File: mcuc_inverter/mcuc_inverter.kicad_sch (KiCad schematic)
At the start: 0 parts

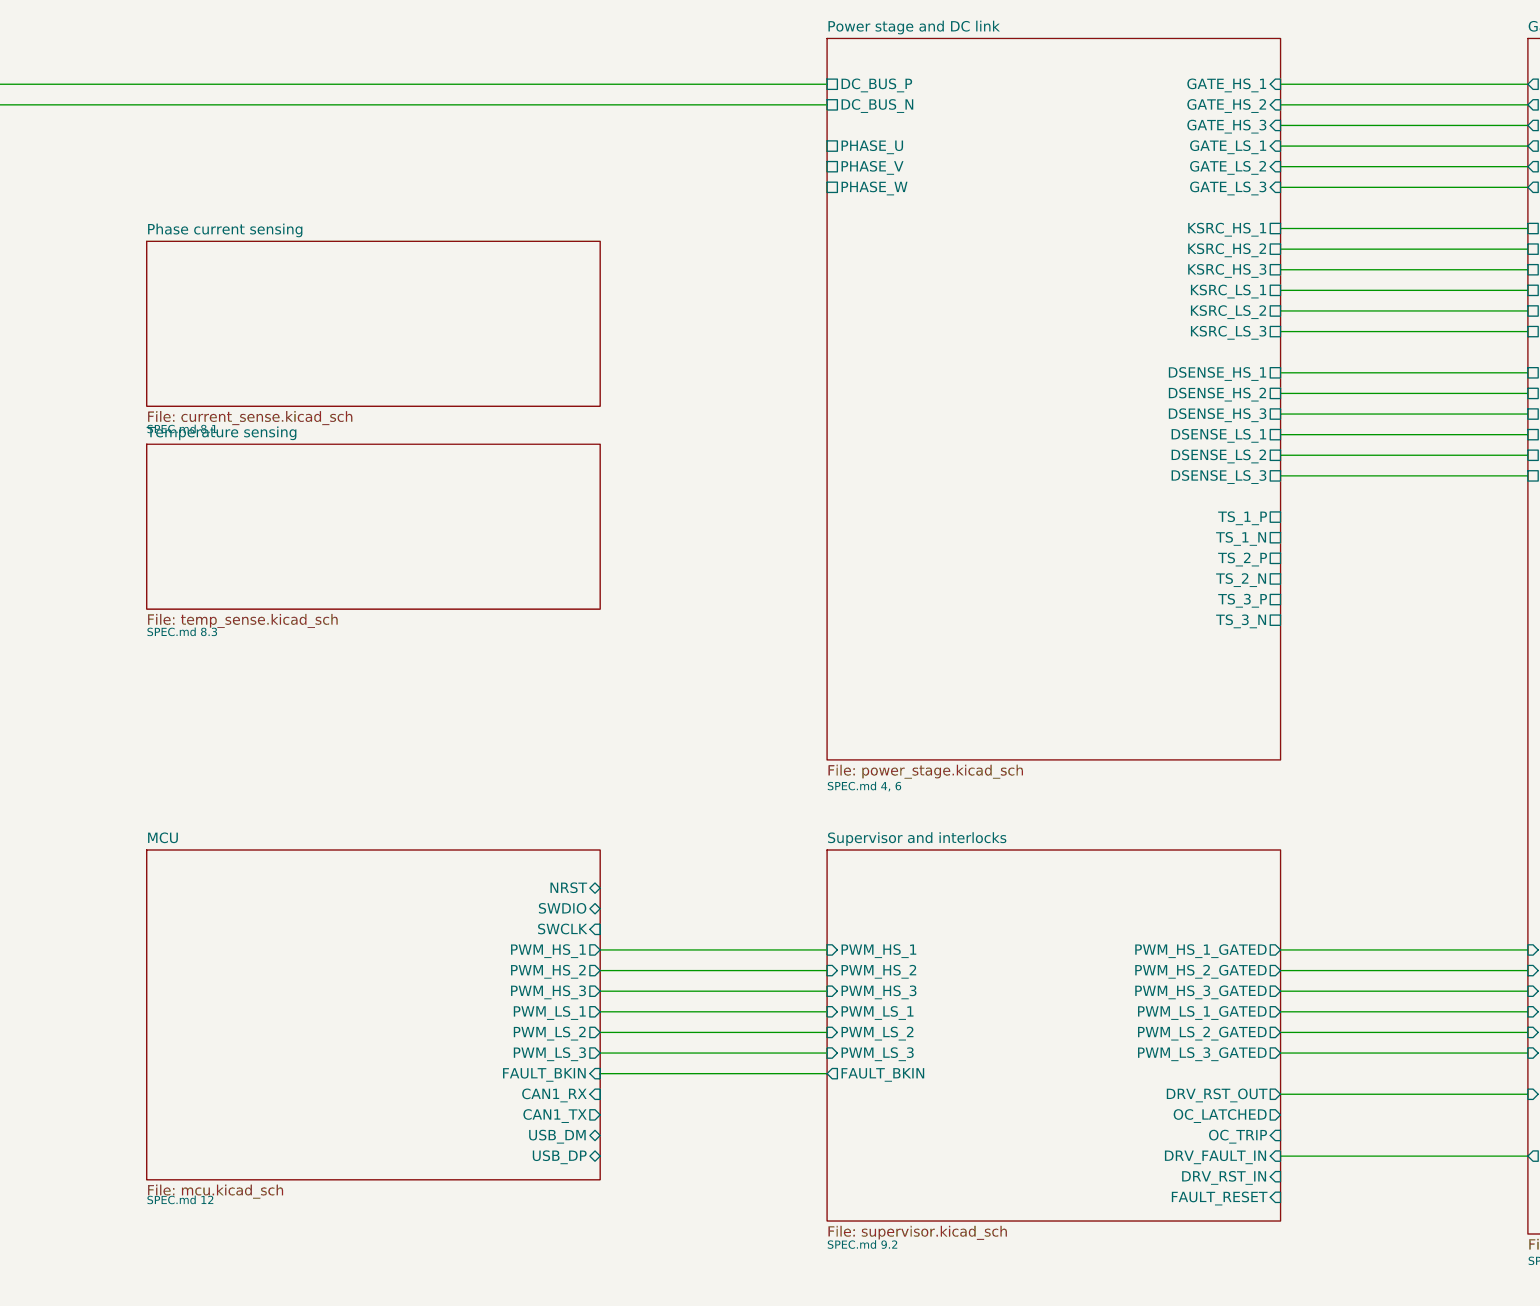
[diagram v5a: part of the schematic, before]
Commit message: Capture current_sense sheet: 3x HOYS 200-S/SP33 + 300 A trip
Per D019: LEM HOYS transducers with explicit primary pins so the
phase busbar path is in the netlist (U201 phase terminal -> P1/P2 ->
PHASE_x_OUT). Pinout verified from the LEM datasheet connection
figure - 5-pin device including an OCD output the brief didn't know
about, wire-OR'd onto OC_TRIP as an independent ~584 A backup trip.

Per phase: 100R/1nF anti-alias to I_PH_x, individual I_REF_x (Uref
outputs may not be paralleled per datasheet), and an LM2903-class
open-drain window comparator pair (thresholds 2.340/0.960 V from a
9.53k/13.7k/9.53k E96 string = +/-300 A at 2.3 mV/A) pulling
OC_TRIP low on either polarity - matching the ported PALTA
active-low wired-OR into R907 + the supervisor edge-maker. No
hysteresis by design: the supervisor latches the first edge; note
on-sheet.

Root: PHASE_U/V/W wired power_stage -> current_sense; OC_TRIP wired
to supervisor. ERC 0 errors; 69/69 netlist checks by the agent;
OC_TRIP membership (exactly 11 nodes) and phase continuity
independently re-verified.

Co-Authored-By: Claude Fable 5 <noreply@anthropic.com>
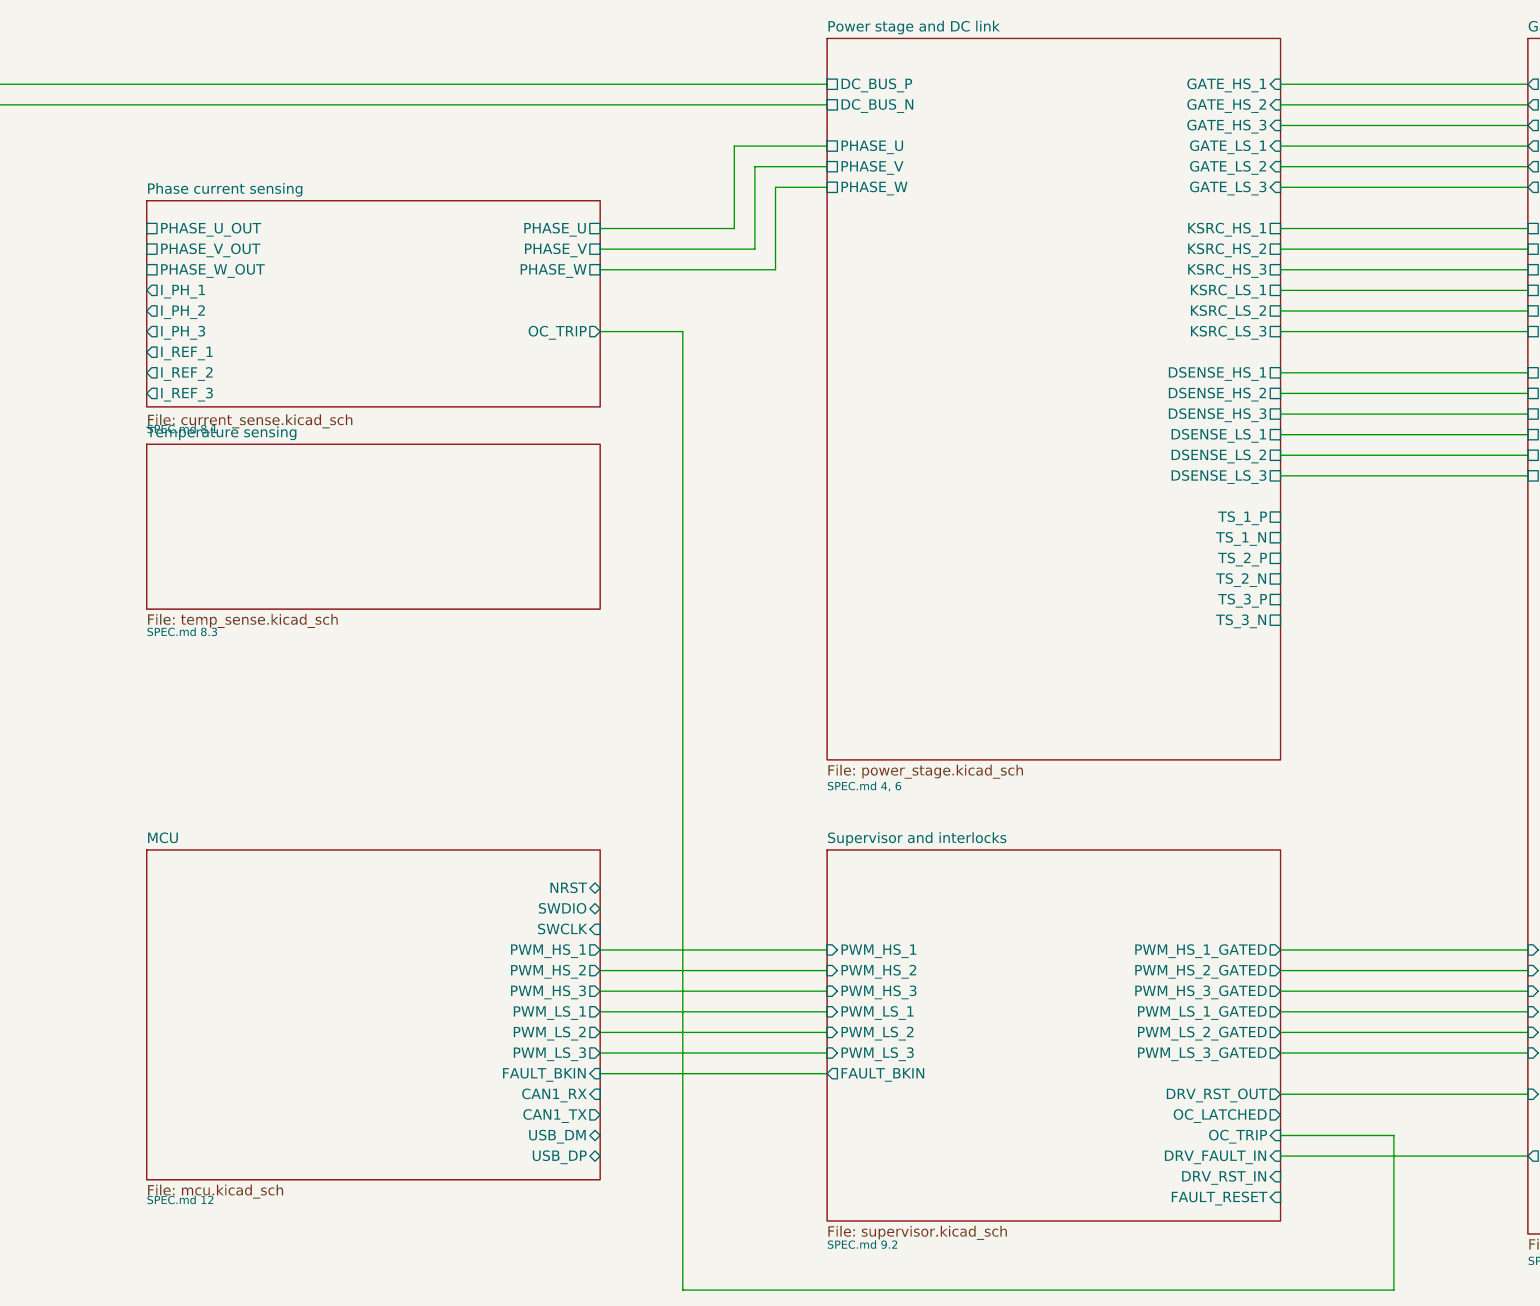
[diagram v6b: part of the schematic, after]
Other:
- sheet Phase current sensing ports: added I_PH_1, I_PH_2, I_PH_3, I_REF_1, I_REF_2, I_REF_3, OC_TRIP, PHASE_U, PHASE_U_OUT, PHASE_V, PHASE_V_OUT, PHASE_W, PHASE_W_OUT; removed none

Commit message: Capture aux_power sheet: full D020 rail tree, 7 blocks
INN3990CQ flyback per datasheet Fig. 10 / DER-948Q (series-string
input films, RCD clamp, custom 3-winding transformer symbol with
Lp/VOR/isolation notes, bias->BPP, Schottky secondary, FB 143k/13.2k
-> 14.97 V, SR and IS tied to GND per datasheet for diode operation);
LM5175 buck-boost aux path (15.02 V, deliberately above the
diode-dropped flyback so aux carries the load when present) through
LM74610-Q1 + external FET; two LMR51430 bucks (5 V: 71.5k/9.76k;
12 V: 115k/6.04k); TLV1117-33 3.3 V (PWR_FLAG moved here from the
MCU sheet - this is the rail's true source); 4x SN6505B + WE
750316856 gate supplies (winding CT pinout verified from the WE
drawing; +17.9/-5.1 zener splits); NXE2S0505MC isolated CAN 5 V.

All 12 VGD nets verified in the netlist to span aux_power sources
and gate_drive loads (e.g. VGD_HS1_P = rectifiers + caps + U301
VCC2), independently re-checked before commit. ERC 0 errors.

Co-Authored-By: Claude Fable 5 <noreply@anthropic.com>
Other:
- sheet Auxiliary power ports: added AUX_IN, CAN_5V, CAN_GND, DC_BUS_N, DC_BUS_P, VGD_HS1_COM, VGD_HS1_N, VGD_HS1_P, VGD_HS2_COM, VGD_HS2_N, VGD_HS2_P, VGD_HS3_COM, VGD_HS3_N, VGD_HS3_P, VGD_LS_COM, VGD_LS_N, VGD_LS_P; removed none
- note added: "AUX_IN: external 12-24 V feed (connector on comms/IO sheet, TBD). VGD_* nets: net-labelled to the gate_drive sheet pins on the right."

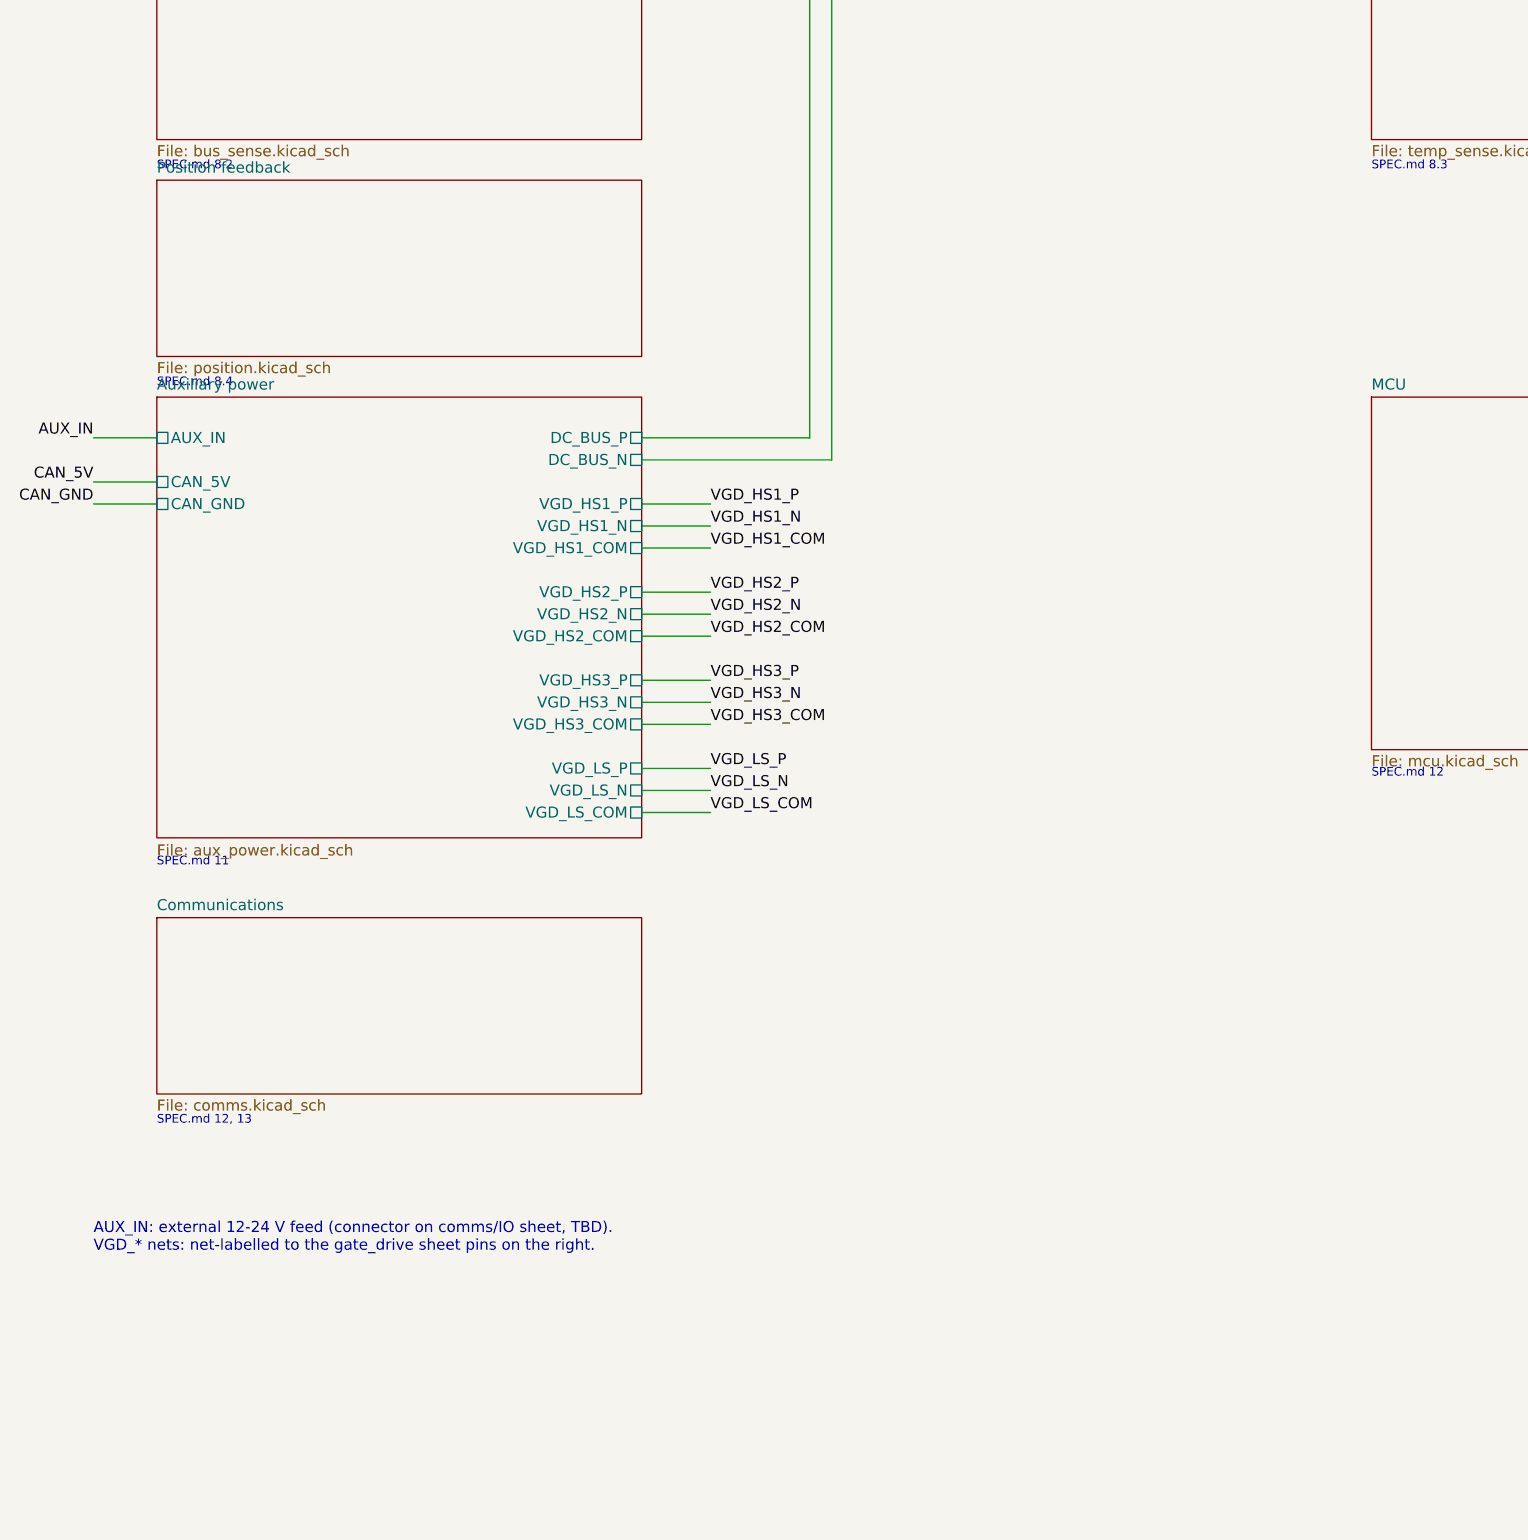
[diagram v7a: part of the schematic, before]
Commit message: Capture position sheet: AD2S1205 resolver, halls, encoder, SinCos
Port from PALTA legacy sheets, verified pin-by-pin against the ADI
datasheet and the legacy VESC-controller.net (175/175 netlist
checks). Fixes two legacy defects found during reconstruction: SOE
(serial output enable, an INPUT mislabeled as output in the legacy
symbol) was left floating on PALTA - now tied low for serial mode;
and the A/B/NM encoder-emulation outputs that make VESC resolver
support free (D003) were never wired on the legacy board - now
brought out via 0R links with an exclusive-population note vs the
external ABI encoder. REFBYP decoupling added per datasheet (PALTA
floated pin 43).

Exciter (AD8397), hall clamps (10k + BAT54S, PALTA-faithful, DNP
pullup sites), encoder inputs replicating the hall pattern, SinCos
from the PALTA analog-input pattern, motor temp bias per D022
(resistor-selectable). APX809-46 5V supervisor for AD2S1205 RESET.
8 MHz -> 8.192 MHz crystal correction per datasheet nominal.

ERC 0 errors on root hierarchy.

Co-Authored-By: Claude Fable 5 <noreply@anthropic.com>
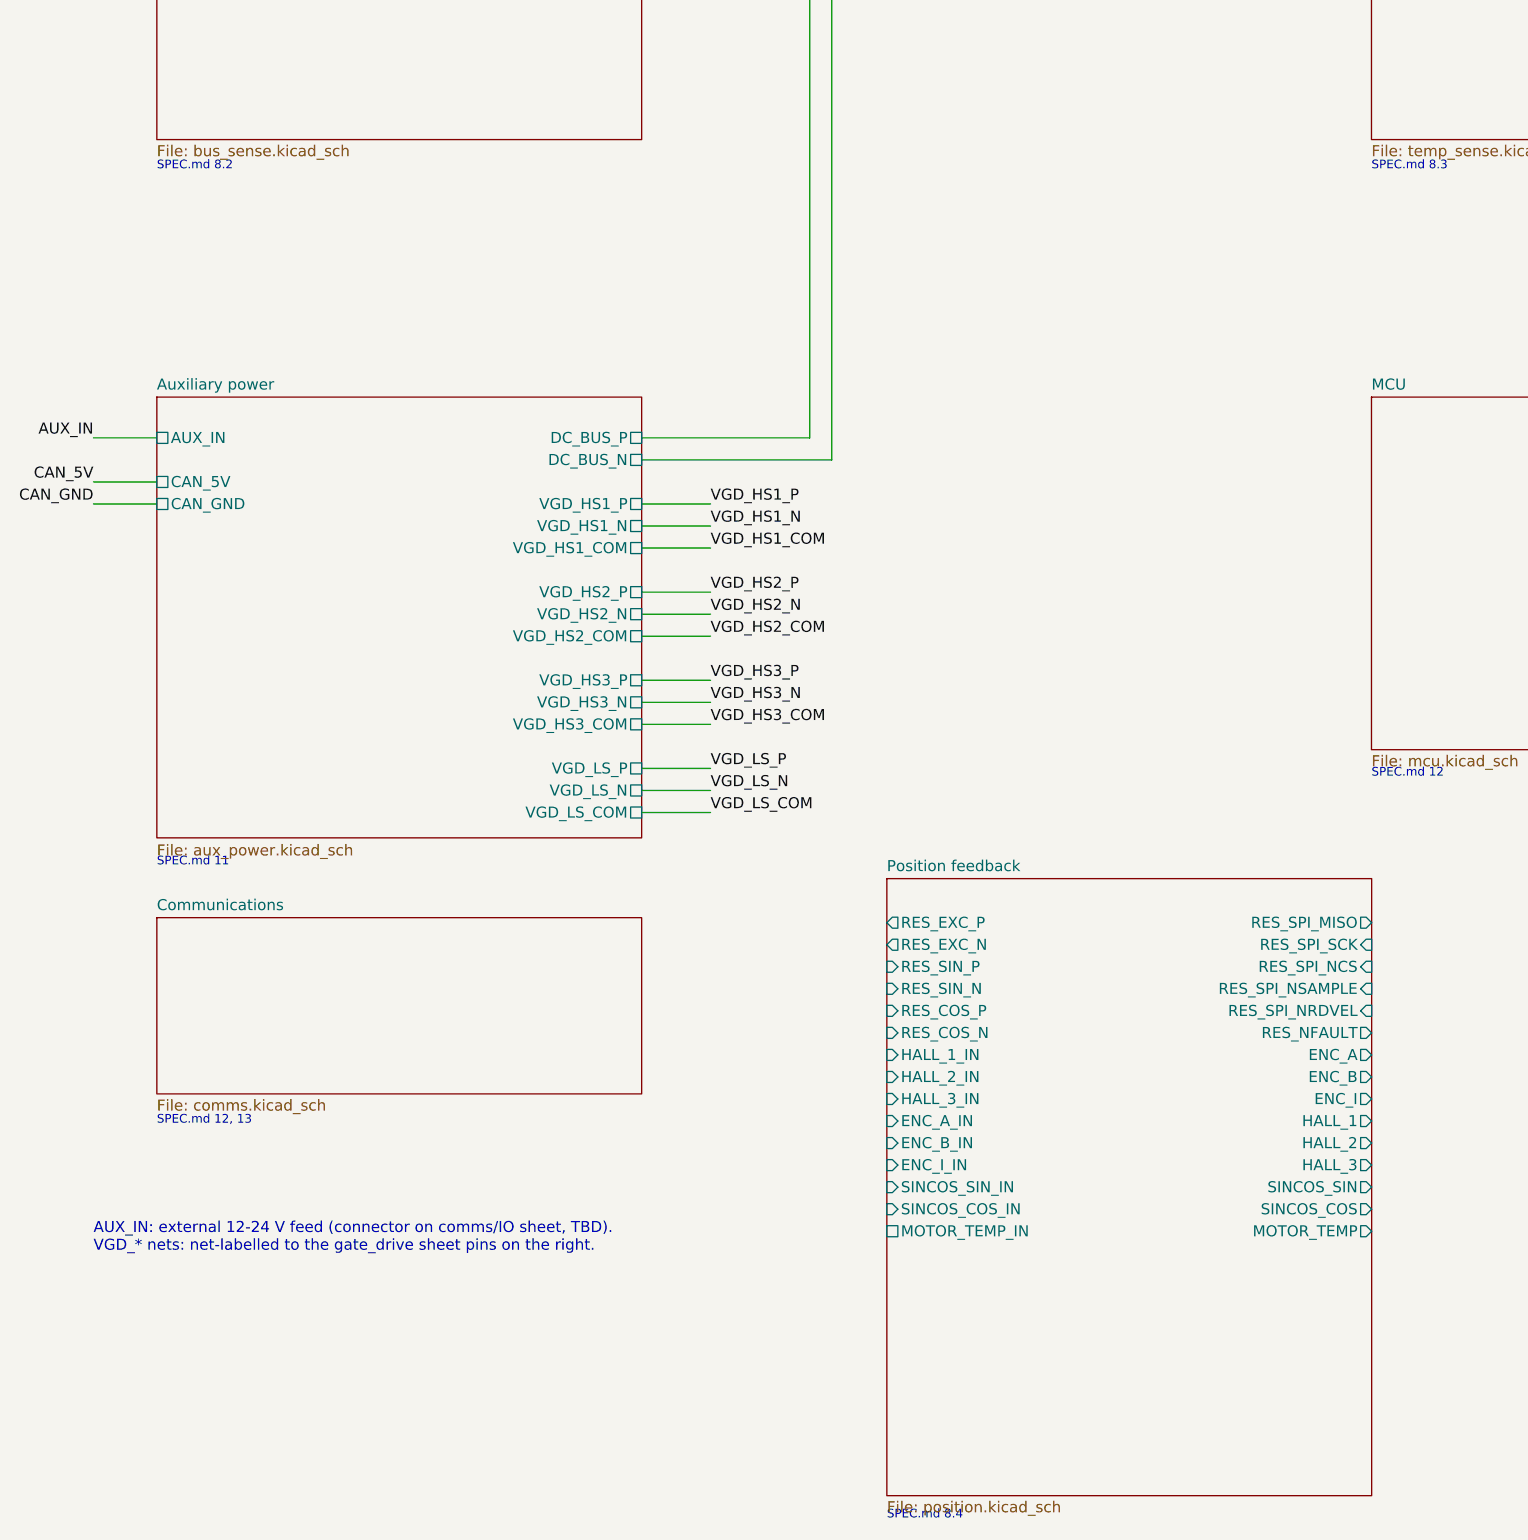
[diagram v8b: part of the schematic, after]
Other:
- sheet Position feedback ports: added ENC_A, ENC_A_IN, ENC_B, ENC_B_IN, ENC_I, ENC_I_IN, HALL_1, HALL_1_IN, HALL_2, HALL_2_IN, HALL_3, HALL_3_IN, MOTOR_TEMP, MOTOR_TEMP_IN, RES_COS_N, RES_COS_P, RES_EXC_N, RES_EXC_P, RES_NFAULT, RES_SIN_N, RES_SIN_P, RES_SPI_MISO, RES_SPI_NCS, RES_SPI_NRDVEL, RES_SPI_NSAMPLE, RES_SPI_SCK, SINCOS_COS, SINCOS_COS_IN, SINCOS_SIN, SINCOS_SIN_IN; removed none
